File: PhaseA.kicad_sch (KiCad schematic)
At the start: 12 parts, among them Q10 Q_NMOS, Q9 Q_NMOS, U2 STDriveG600

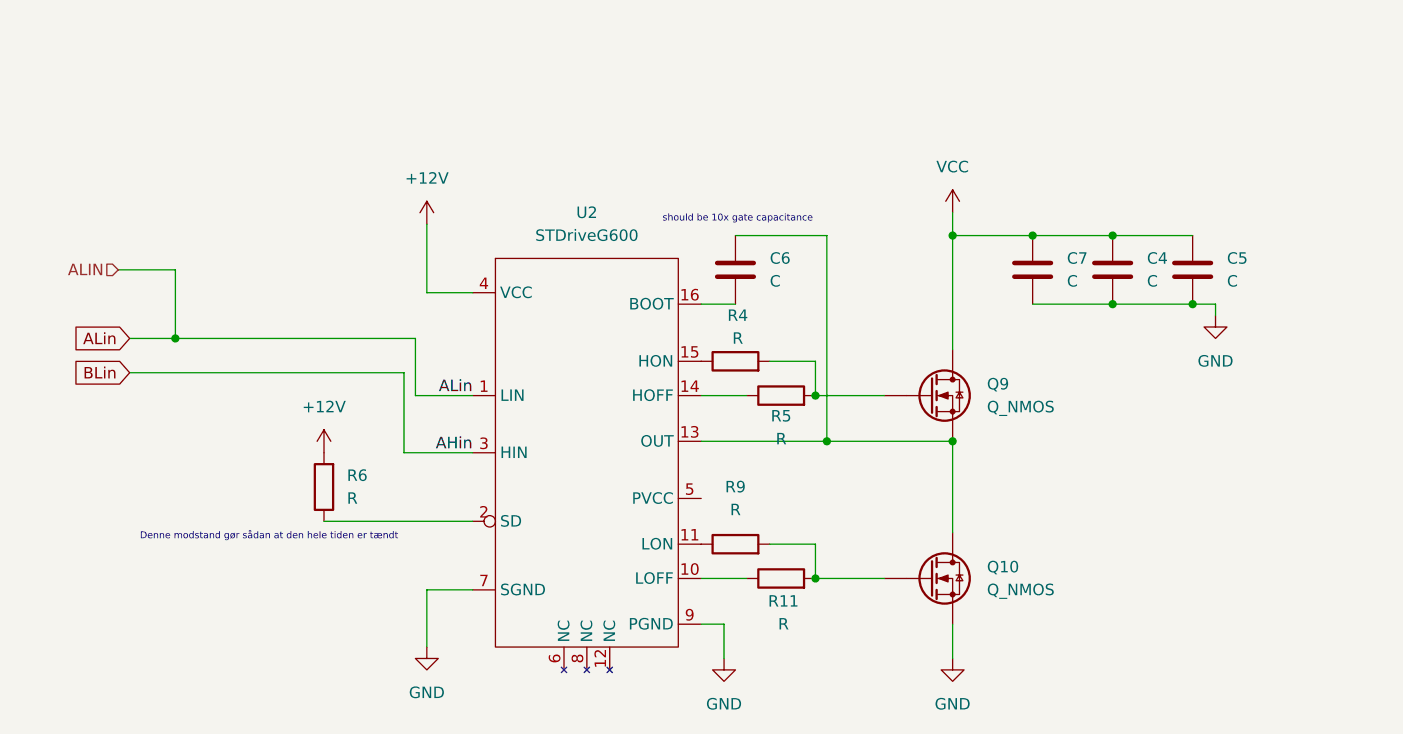
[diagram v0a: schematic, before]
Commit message: added more data for the 3 Phases. also added transformer
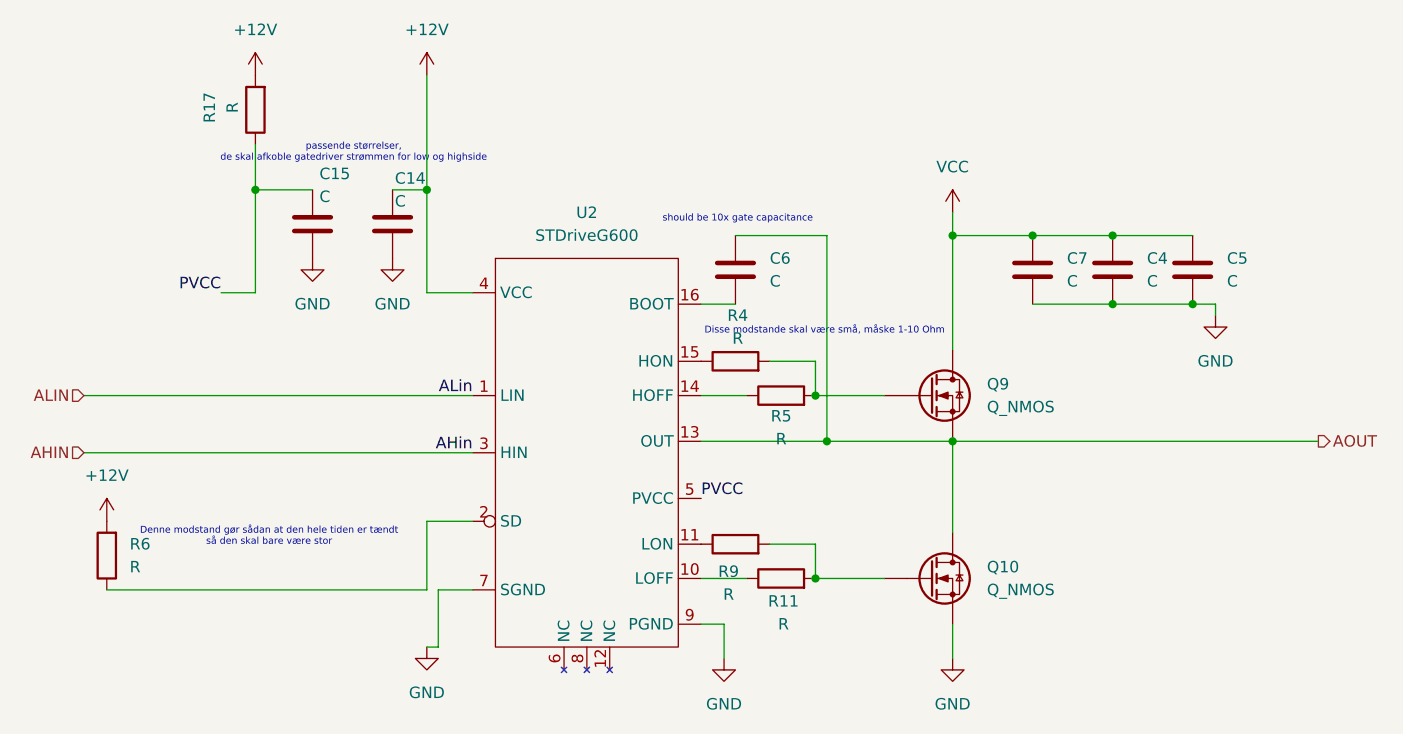
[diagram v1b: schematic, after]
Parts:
- added C14, C15: C, symbol Device:C
- added R17: R, symbol Device:R
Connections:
- net +12V: now also C14.1, R17.2
- net GND: now also C14.2, C15.2
- net AOUT: now reaches C6.1, Q10.D, Q9.S, U2.13 (OUT)
- net PVCC: now reaches U2.5 (PVCC)
- net PVCC: now also C15.1, R17.1
- net ALin renamed ALIN
- net BLin renamed AHIN
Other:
- note added: "Denne modstand gør sådan at den hele tiden er tændt så den skal bare være stor"
- note added: "Disse modstande skal være små, måske 1-10 Ohm"
- note added: "passende størrelser, de skal afkoble gatedriver strømmen for low og highside"
- note removed: "Denne modstand gør sådan at den hele tiden er tændt"
- moved on the sheet: R6

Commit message: small changes
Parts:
- C14, C15, C7: value C -> 10u
- C4, C5: value C -> 100u
- C6: value C -> 470n
- R17: value R -> 3
- R6: value R -> 10k
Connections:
- net VCC renamed +48V
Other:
- note added: "flere typer kapacitorer husk strømvejen"
- note added: "should be 10x gate capacitance husk LAV ESR så nok MLCC X7R"
- note removed: "should be 10x gate capacitance"
- moved on the sheet: C4, C5
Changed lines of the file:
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@@
 	(generator_version "9.0")
 	(paper "A4")
-	(text "Disse modstande skal være små, måske 1-10 Ohm"
-		(exclude_from_sim no)
-		(at 158.496 62.738 0)
+	(text "Disse modstande skal være små, \nmåske 1-10 Ohm"
+		(exclude_from_sim no)
+		(at 156.718 76.962 0)
+		(effects
+			(font
+				(size 0.762 0.762)
+			)
+		)
+	)
+	(text "flere typer kapacitorer\nhusk strømvejen"
+		(exclude_from_sim no)
+		(at 191.516 48.006 0)
 		(effects
 			(font
@@
 		)
 	)
-	(text "should be 10x gate capacitance\n"
-		(exclude_from_sim no)
-		(at 148.844 50.292 0)
+	(text "should be 10x gate capacitance\nhusk LAV ESR så nok MLCC X7R\n"
+		(exclude_from_sim no)
+		(at 150.876 50.292 0)
 		(effects
 			(font
@@
 	)
 	(junction
-		(at 190.5 52.07)
+		(at 181.61 52.07)
 		(diameter 0)
 		(color 0 0 0 0)
 	)
 	(junction
-		(at 181.61 52.07)
+		(at 191.77 59.69)
+		(diameter 0)
+		(color 0 0 0 0)
+	)
+	(junction
+		(at 203.2 59.69)
 		(diameter 0)
 		(color 0 0 0 0)
@@
 	)
 	(junction
+		(at 191.77 52.07)
+		(diameter 0)
+		(color 0 0 0 0)
+	)
+	(junction
 		(at 157.48 90.17)
 		(diameter 0)
@@
 	)
 	(junction
-		(at 190.5 59.69)
-		(diameter 0)
-		(color 0 0 0 0)
-	)
-	(junction
-		(at 199.39 59.69)
-		(diameter 0)
-		(color 0 0 0 0)
-	)
-	(junction
 		(at 95.25 46.99)
 		(diameter 0)
@@
 	(wire
 		(pts
-			(xy 181.61 59.69) (xy 190.5 59.69)
+			(xy 191.77 59.69) (xy 203.2 59.69)
+		)
+		(stroke
+			(width 0)
+			(type default)
+		)
+	)
+	(wire
+		(pts
+			(xy 181.61 59.69) (xy 191.77 59.69)
 		)
 		(stroke
@@
 	(wire
 		(pts
-			(xy 190.5 52.07) (xy 199.39 52.07)
-		)
-		(stroke
-			(width 0)
-			(type default)
-		)
-	)
-	(wire
-		(pts
-			(xy 199.39 59.69) (xy 201.93 59.69)
-		)
-		(stroke
-			(width 0)
-			(type default)
-		)
-	)
-	(wire
-		(pts
-			(xy 181.61 52.07) (xy 190.5 52.07)
+			(xy 191.77 52.07) (xy 203.2 52.07)
+		)
+		(stroke
+			(width 0)
+			(type default)
+		)
+	)
+	(wire
+		(pts
+			(xy 181.61 52.07) (xy 191.77 52.07)
 		)
 		(stroke
@@
 	(wire
 		(pts
-			(xy 190.5 59.69) (xy 199.39 59.69)
+			(xy 207.01 59.69) (xy 203.2 59.69)
 		)
 		(stroke
@@
 	(wire
 		(pts
-			(xy 201.93 59.69) (xy 201.93 60.96)
+			(xy 207.01 59.69) (xy 207.01 60.96)
 		)
 		(stroke
@@
 			)
 		)
-		(property "Value" "C"
+		(property "Value" "470n"
 			(at 152.4 57.1499 0)
 			(effects
@@
 			)
 		)
-		(property "Value" "C"
+		(property "Value" "10u"
 			(at 185.42 57.1499 0)
 			(effects
@@
 	)
 	(symbol
+		(lib_id "power:+48V")
+		(at 172.72 49.53 0)
+		(unit 1)
+		(exclude_from_sim no)
+		(in_bom yes)
+		(on_board yes)
+		(dnp no)
+		(fields_autoplaced yes)
+		(property "Reference" "#PWR014"
+			(at 172.72 53.34 0)
+			(effects
+				(font
+					(size 1.27 1.27)
+				)
+				(hide yes)
+			)
+		)
+		(property "Value" "+48V"
+			(at 172.72 44.45 0)
+			(effects
+				(font
+					(size 1.27 1.27)
+				)
+			)
+		)
+		(property "Footprint" ""
+			(at 172.72 49.53 0)
+			(effects
+				(font
+					(size 1.27 1.27)
+				)
+				(hide yes)
+			)
+		)
+		(property "Datasheet" ""
+			(at 172.72 49.53 0)
+			(effects
+				(font
+					(size 1.27 1.27)
+				)
+				(hide yes)
+			)
+		)
+		(property "Description" "Power symbol creates a global label with name \"+48V\""
+			(at 172.72 49.53 0)
+			(effects
+				(font
+					(size 1.27 1.27)
+				)
+				(hide yes)
+			)
+		)
+		(pin "1"
+		)
+		(instances
+			(project "BachelorCurrentTripler"
+				(path "/eaeaab39-7712-4bb8-8f1a-3ddca096a313/599aab1d-92e3-47b4-80e6-e5f9d8661647"
+					(reference "#PWR014")
+					(unit 1)
+				)
+			)
+		)
+	)
+	(symbol
 		(lib_id "Device:R")
 		(at 153.67 69.85 90)
@@
 		)
 		(property "Value" "R"
-			(at 153.67 74.676 90)
+			(at 153.67 73.914 90)
 			(effects
 				(font
@@
 			)
 		)
-		(property "Value" "R"
+		(property "Value" "10k"
 			(at 81.28 88.8999 0)
 			(effects
@@
 				(path "/eaeaab39-7712-4bb8-8f1a-3ddca096a313/599aab1d-92e3-47b4-80e6-e5f9d8661647"
 					(reference "R6")
-					(unit 1)
-				)
-			)
-		)
-	)
-	(symbol
-		(lib_id "power:VCC")
-		(at 172.72 49.53 0)
-		(unit 1)
-		(exclude_from_sim no)
-		(in_bom yes)
-		(on_board yes)
-		(dnp no)
-		(fields_autoplaced yes)
-		(property "Reference" "#PWR014"
-			(at 172.72 53.34 0)
-			(effects
-				(font
-					(size 1.27 1.27)
-				)
-				(hide yes)
-			)
-		)
-		(property "Value" "VCC"
-			(at 172.72 44.45 0)
-			(effects
-				(font
-					(size 1.27 1.27)
-				)
-			)
-		)
-		(property "Footprint" ""
-			(at 172.72 49.53 0)
-			(effects
-				(font
-					(size 1.27 1.27)
-				)
-				(hide yes)
-			)
-		)
-		(property "Datasheet" ""
-			(at 172.72 49.53 0)
-			(effects
-				(font
-					(size 1.27 1.27)
-				)
-				(hide yes)
-			)
-		)
-		(property "Description" "Power symbol creates a global label with name \"VCC\""
-			(at 172.72 49.53 0)
-			(effects
-				(font
-					(size 1.27 1.27)
-				)
-				(hide yes)
-			)
-		)
-		(pin "1"
-		)
-		(instances
-			(project ""
-				(path "/eaeaab39-7712-4bb8-8f1a-3ddca096a313/599aab1d-92e3-47b4-80e6-e5f9d8661647"
-					(reference "#PWR014")
 					(unit 1)
 				)
@@
 	(symbol
 		(lib_id "power:GND")
-		(at 201.93 60.96 0)
+		(at 207.01 60.96 0)
 		(unit 1)
 		(exclude_from_sim no)
@@
 		(fields_autoplaced yes)
 		(property "Reference" "#PWR07"
-			(at 201.93 67.31 0)
+			(at 207.01 67.31 0)
 			(effects
 				(font
@@
 		)
 		(property "Value" "GND"
-			(at 201.93 66.04 0)
-			(effects
-				(font
-					(size 1.27 1.27)
-				)
-			)
-		)
-		(property "Footprint" ""
-			(at 201.93 60.96 0)
+			(at 207.01 66.04 0)
+			(effects
+				(font
+					(size 1.27 1.27)
+				)
+			)
+		)
+		(property "Footprint" ""
+			(at 207.01 60.96 0)
 			(effects
 				(font
@@
 		)
 		(property "Datasheet" ""
-			(at 201.93 60.96 0)
+			(at 207.01 60.96 0)
 			(effects
 				(font
@@
 		)
 		(property "Description" "Power symbol creates a global label with name \"GND\" , ground"
-			(at 201.93 60.96 0)
+			(at 207.01 60.96 0)
 			(effects
 				(font
@@
 			)
 		)
-		(property "Value" "C"
+		(property "Value" "10u"
 			(at 102.362 47.752 0)
 			(effects
@@
 	(symbol
 		(lib_id "Device:C")
-		(at 199.39 55.88 0)
+		(at 203.2 55.88 0)
 		(unit 1)
 		(exclude_from_sim no)
@@
 		(fields_autoplaced yes)
 		(property "Reference" "C5"
-			(at 203.2 54.6099 0)
+			(at 207.01 54.6099 0)
 			(effects
 				(font
@@
 			)
 		)
-		(property "Value" "C"
-			(at 203.2 57.1499 0)
+		(property "Value" "100u"
+			(at 207.01 57.1499 0)
 			(effects
 				(font
@@
 		)
 		(property "Footprint" ""
-			(at 200.3552 59.69 0)
+			(at 204.1652 59.69 0)
 			(effects
 				(font
@@
 		)
 		(property "Datasheet" "~"
-			(at 199.39 55.88 0)
+			(at 203.2 55.88 0)
 			(effects
 				(font
@@
 		)
 		(property "Description" "Unpolarized capacitor"
-			(at 199.39 55.88 0)
+			(at 203.2 55.88 0)
 			(effects
 				(font
@@
 			)
 		)
-		(property "Value" "R"
+		(property "Value" "3"
 			(at 92.71 37.846 90)
 			(effects
@@
 			)
 		)
-		(property "Value" "C"
+		(property "Value" "10u"
 			(at 110.744 48.26 0)
 			(effects
@@
 	(symbol
 		(lib_id "Device:C")
-		(at 190.5 55.88 0)
+		(at 191.77 55.88 0)
 		(unit 1)
 		(exclude_from_sim no)
@@
 		(fields_autoplaced yes)
 		(property "Reference" "C4"
-			(at 194.31 54.6099 0)
+			(at 195.58 54.6099 0)
 			(effects
 				(font
@@
 			)
 		)
-		(property "Value" "C"
-			(at 194.31 57.1499 0)
+		(property "Value" "100u"
+			(at 195.58 57.1499 0)
 			(effects
 				(font
@@
 		)
 		(property "Footprint" ""
-			(at 191.4652 59.69 0)
+			(at 192.7352 59.69 0)
 			(effects
 				(font
@@
 		)
 		(property "Datasheet" "~"
-			(at 190.5 55.88 0)
+			(at 191.77 55.88 0)
 			(effects
 				(font
@@
 		)
 		(property "Description" "Unpolarized capacitor"
-			(at 190.5 55.88 0)
-			(effects
-				(font
+			(at 191.77 55.88 0)
+			(effects
+				(font

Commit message: added some kind of PCB design, a rough draft
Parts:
- removed Q10, Q9: Q_NMOS, symbol Device:Q_NMOS
- added Q13, Q7: C2M0025120D, Package_TO_SOT_THT:TO-247-3_Vertical, symbol Transistor_FET:C2M0025120D
- C2: renamed from C15; footprint (none) -> Capacitor_SMD:C_1812_4532Metric
- C3: renamed from C14; footprint (none) -> Capacitor_SMD:C_1812_4532Metric
- C4: renamed from C6; footprint (none) -> Capacitor_SMD:C_1206_3216Metric
- C5: renamed from C7; footprint (none) -> Capacitor_SMD:C_2220_5750Metric
- C6: renamed from C4; footprint (none) -> Capacitor_SMD:C_Elec_6.3x7.7
- C7: renamed from C5; footprint (none) -> Capacitor_SMD:C_Elec_6.3x7.7
- R2: renamed from R17; footprint (none) -> Resistor_SMD:R_1210_3225Metric
- R3: renamed from R4; footprint (none) -> Resistor_SMD:R_1206_3216Metric
- R4: renamed from R5; footprint (none) -> Resistor_SMD:R_1206_3216Metric
- R5: renamed from R9; footprint (none) -> Resistor_SMD:R_1206_3216Metric
- R6: footprint (none) -> Resistor_SMD:R_1812_4532Metric
- R7: renamed from R11; footprint (none) -> Resistor_SMD:R_1206_3216Metric
- renumbered U2 to U1
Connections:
- net +48V: now also Q7.2 (D)
- net AOUT: now also Q13.2 (D), Q7.3 (S)
- net GND: now also Q13.3 (S)
- net at R3.2, R4.2: now also Q7.1 (G)
- net at R5.2, R7.2: now also Q13.1 (G)

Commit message: intial pcb layout
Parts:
- Q13, Q7: footprint Package_TO_SOT_THT:TO-247-3_Vertical -> Package_TO_SOT_SMD:TO-252-2
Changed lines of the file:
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@@
 			)
 		)
-		(property "Footprint" "Package_TO_SOT_THT:TO-247-3_Vertical"
+		(property "Footprint" "Package_TO_SOT_SMD:TO-252-2"
 			(at 175.26 92.075 0)
 			(effects
@@
 			)
 		)
-		(property "Footprint" "Package_TO_SOT_THT:TO-247-3_Vertical"
+		(property "Footprint" "Package_TO_SOT_SMD:TO-252-2"
 			(at 175.26 71.755 0)
 			(effects

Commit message: local restore changes
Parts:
- C2, C3: LCSC Part Number (none) -> C1021609
- C4: LCSC Part Number (none) -> C507059
- C5: LCSC Part Number (none) -> C2843466
- C6: value 100u -> 47u; footprint Capacitor_SMD:C_Elec_6.3x7.7 -> easyeda:CAP-SMD_BD6.3-L6.6-W6.6-LS7.3-FD; LCSC Part Number (none) -> C7461235
- C7: footprint Capacitor_SMD:C_Elec_6.3x7.7 -> easyeda:CAP-SMD_BD8.0-L8.3-W8.3-LS9.2-FD-H10.5; LCSC Part Number (none) -> C5456764
- Q13, Q7, R3, R4, R5, R7: now left out of the parts list
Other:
- note added: "Disse modstande skal være små, måske 1-10 Ohm 0805 størrelse sortimentskasser i mice ?"
- note removed: "Disse modstande skal være små, måske 1-10 Ohm"
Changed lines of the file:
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@@
 	(generator_version "9.0")
 	(paper "A4")
-	(text "Disse modstande skal være små, \nmåske 1-10 Ohm"
-		(exclude_from_sim no)
-		(at 156.718 76.962 0)
+	(text "Disse modstande skal være små, \nmåske 1-10 Ohm\n\n0805 størrelse\n\nsortimentskasser i mice ?"
+		(exclude_from_sim no)
+		(at 158.496 78.74 0)
 		(effects
 			(font
@@
 			)
 		)
+		(property "LCSC Part Number" "C507059"
+			(at 148.59 55.88 0)
+			(effects
+				(font
+					(size 1.27 1.27)
+				)
+				(hide yes)
+			)
+		)
 		(pin "2"
 		)
@@
 			)
 		)
+		(property "LCSC Part Number" "C2843466 "
+			(at 181.61 55.88 0)
+			(effects
+				(font
+					(size 1.27 1.27)
+				)
+				(hide yes)
+			)
+		)
 		(pin "1"
 		)
@@
 		(unit 1)
 		(exclude_from_sim no)
-		(in_bom yes)
+		(in_bom no)
 		(on_board yes)
 		(dnp no)
@@
 		(unit 1)
 		(exclude_from_sim no)
-		(in_bom yes)
+		(in_bom no)
 		(on_board yes)
 		(dnp no)
@@
 		(unit 1)
 		(exclude_from_sim no)
-		(in_bom yes)
+		(in_bom no)
 		(on_board yes)
 		(dnp no)
@@
 			)
 		)
+		(property "LCSC Part Number" "C1021609"
+			(at 101.6 50.8 0)
+			(effects
+				(font
+					(size 1.27 1.27)
+				)
+				(hide yes)
+			)
+		)
 		(pin "2"
 		)
@@
 			)
 		)
-		(property "Footprint" "Capacitor_SMD:C_Elec_6.3x7.7"
+		(property "Footprint" "easyeda:CAP-SMD_BD8.0-L8.3-W8.3-LS9.2-FD-H10.5"
 			(at 204.1652 59.69 0)
 			(effects
@@
 			)
 		)
+		(property "LCSC Part Number" "C5456764"
+			(at 203.2 55.88 0)
+			(effects
+				(font
+					(size 1.27 1.27)
+				)
+				(hide yes)
+			)
+		)
 		(pin "1"
 		)
@@
 		(unit 1)
 		(exclude_from_sim no)
-		(in_bom yes)
+		(in_bom no)
 		(on_board yes)
 		(dnp no)
@@
 		(unit 1)
 		(exclude_from_sim no)
-		(in_bom yes)
+		(in_bom no)
 		(on_board yes)
 		(dnp no)
@@
 		(unit 1)
 		(exclude_from_sim no)
-		(in_bom yes)
+		(in_bom no)
 		(on_board yes)
 		(dnp no)
@@
 			)
 		)
+		(property "LCSC Part Number" "C1021609"
+			(at 110.49 50.8 0)
+			(effects
+				(font
+					(size 1.27 1.27)
+				)
+				(hide yes)
+			)
+		)
 		(pin "2"
 		)
@@
 			)
 		)
-		(property "Value" "100u"
+		(property "Value" "47u"
 			(at 195.58 57.1499 0)
 			(effects
@@
 			)
 		)
-		(property "Footprint" "Capacitor_SMD:C_Elec_6.3x7.7"
+		(property "Footprint" "easyeda:CAP-SMD_BD6.3-L6.6-W6.6-LS7.3-FD"
 			(at 192.7352 59.69 0)
 			(effects
@@
 			(at 191.77 55.88 0)
 			(effects
+				(font
+					(size 1.27 1.27)
+				)
+				(hide yes)
+			)
+		)
+		(property "LCSC Part Number" "C7461235"
+			(at 191.77 55.88 0)
+			(effects

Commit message: all små komponenter er nu 0805, og jeg har fixet strømmen under kondensatorerene, mangler kun at bytte rundt på 12Vin og GND
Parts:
- C2, C3: footprint Capacitor_SMD:C_1812_4532Metric -> Capacitor_SMD:C_0805_2012Metric_Pad1.18x1.45mm_HandSolder
- C4: footprint Capacitor_SMD:C_1206_3216Metric -> Capacitor_SMD:C_0805_2012Metric_Pad1.18x1.45mm_HandSolder
- R2: footprint Resistor_SMD:R_1210_3225Metric -> Resistor_SMD:R_0805_2012Metric_Pad1.20x1.40mm_HandSolder
- R3, R4, R5, R7: footprint Resistor_SMD:R_1206_3216Metric -> Resistor_SMD:R_0805_2012Metric_Pad1.20x1.40mm_HandSolder
- R6: footprint Resistor_SMD:R_1812_4532Metric -> Resistor_SMD:R_0805_2012Metric_Pad1.20x1.40mm_HandSolder
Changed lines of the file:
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@@
 			)
 		)
-		(property "Footprint" "Capacitor_SMD:C_1206_3216Metric"
+		(property "Footprint" "Capacitor_SMD:C_0805_2012Metric_Pad1.18x1.45mm_HandSolder"
 			(at 149.5552 59.69 0)
 			(effects
@@
 			)
 		)
-		(property "Footprint" "Resistor_SMD:R_1206_3216Metric"
+		(property "Footprint" "Resistor_SMD:R_0805_2012Metric_Pad1.20x1.40mm_HandSolder"
 			(at 153.67 71.628 90)
 			(effects
@@
 			)
 		)
-		(property "Footprint" "Resistor_SMD:R_1812_4532Metric"
+		(property "Footprint" "Resistor_SMD:R_0805_2012Metric_Pad1.20x1.40mm_HandSolder"
 			(at 80.518 87.63 90)
 			(effects
@@
 			)
 		)
-		(property "Footprint" "Capacitor_SMD:C_1812_4532Metric"
+		(property "Footprint" "Capacitor_SMD:C_0805_2012Metric_Pad1.18x1.45mm_HandSolder"
 			(at 102.5652 54.61 0)
 			(effects
@@
 			)
 		)
-		(property "Footprint" "Resistor_SMD:R_1210_3225Metric"
+		(property "Footprint" "Resistor_SMD:R_0805_2012Metric_Pad1.20x1.40mm_HandSolder"
 			(at 97.028 38.1 90)
 			(effects
@@
 			)
 		)
-		(property "Footprint" "Resistor_SMD:R_1206_3216Metric"
+		(property "Footprint" "Resistor_SMD:R_0805_2012Metric_Pad1.20x1.40mm_HandSolder"
 			(at 148.59 88.138 90)
 			(effects
@@
 			)
 		)
-		(property "Footprint" "Resistor_SMD:R_1206_3216Metric"
+		(property "Footprint" "Resistor_SMD:R_0805_2012Metric_Pad1.20x1.40mm_HandSolder"
 			(at 148.59 67.818 90)
 			(effects
@@
 			)
 		)
-		(property "Footprint" "Resistor_SMD:R_1206_3216Metric"
+		(property "Footprint" "Resistor_SMD:R_0805_2012Metric_Pad1.20x1.40mm_HandSolder"
 			(at 153.67 91.948 90)
 			(effects
@@
 			)
 		)
-		(property "Footprint" "Capacitor_SMD:C_1812_4532Metric"
+		(property "Footprint" "Capacitor_SMD:C_0805_2012Metric_Pad1.18x1.45mm_HandSolder"
 			(at 111.4552 54.61 0)
 			(effects

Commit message: Final Value Changes
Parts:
- Q13, Q7: value C2M0025120D -> FDD3672
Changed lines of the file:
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@@
 			)
 		)
-		(property "Value" "C2M0025120D"
+		(property "Value" "FDD3672"
 			(at 176.53 91.4399 0)
 			(effects
@@
 			)
 		)
-		(property "Datasheet" "https://www.wolfspeed.com/media/downloads/161/C2M0025120D.pdf"
+		(property "Datasheet" "https://www.onsemi.com/pdf/datasheet/fdd3672-d.pdf"
 			(at 175.26 93.98 0)
 			(effects
@@
 			)
 		)
-		(property "Description" "90A Id, 1200V Vds, 25mOhm, N-Channel SiC MOSFET, TO-247"
+		(property "Description" ""
 			(at 170.18 90.17 0)
 			(effects
@@
 			)
 		)
-		(property "Value" "C2M0025120D"
+		(property "Value" "FDD3672"
 			(at 176.53 71.1199 0)
 			(effects
@@
 			)
 		)
-		(property "Datasheet" "https://www.wolfspeed.com/media/downloads/161/C2M0025120D.pdf"
+		(property "Datasheet" "https://www.onsemi.com/pdf/datasheet/fdd3672-d.pdf"
 			(at 175.26 73.66 0)
 			(effects
@@
 			)
 		)
-		(property "Description" "90A Id, 1200V Vds, 25mOhm, N-Channel SiC MOSFET, TO-247"
+		(property "Description" ""
 			(at 170.18 69.85 0)
 			(effects
